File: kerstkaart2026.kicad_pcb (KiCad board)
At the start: 2 copper layers, 96 x 98.4 mm, 60 parts, among them SW1 TS-1187A-B-A-B, U1 ATtiny1616-MNR (VQFN-20)

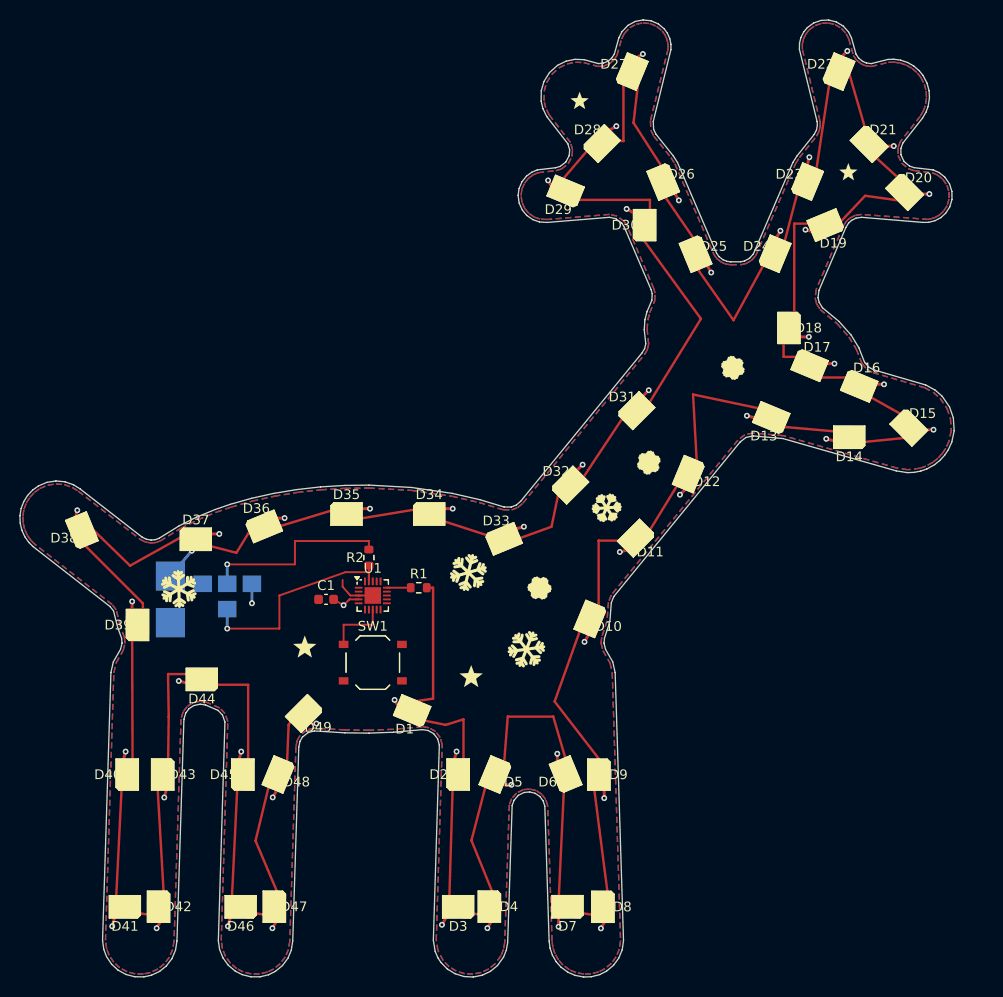
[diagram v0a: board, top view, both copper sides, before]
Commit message: Kerstkaart 2026 v3: SK6805-EC15 LED's, chip als oog, knop als neus, grote batterijpads + JST, rechte LED's, symmetrische geweien
Co-Authored-By: Claude Sonnet 5.5 <noreply@anthropic.com>
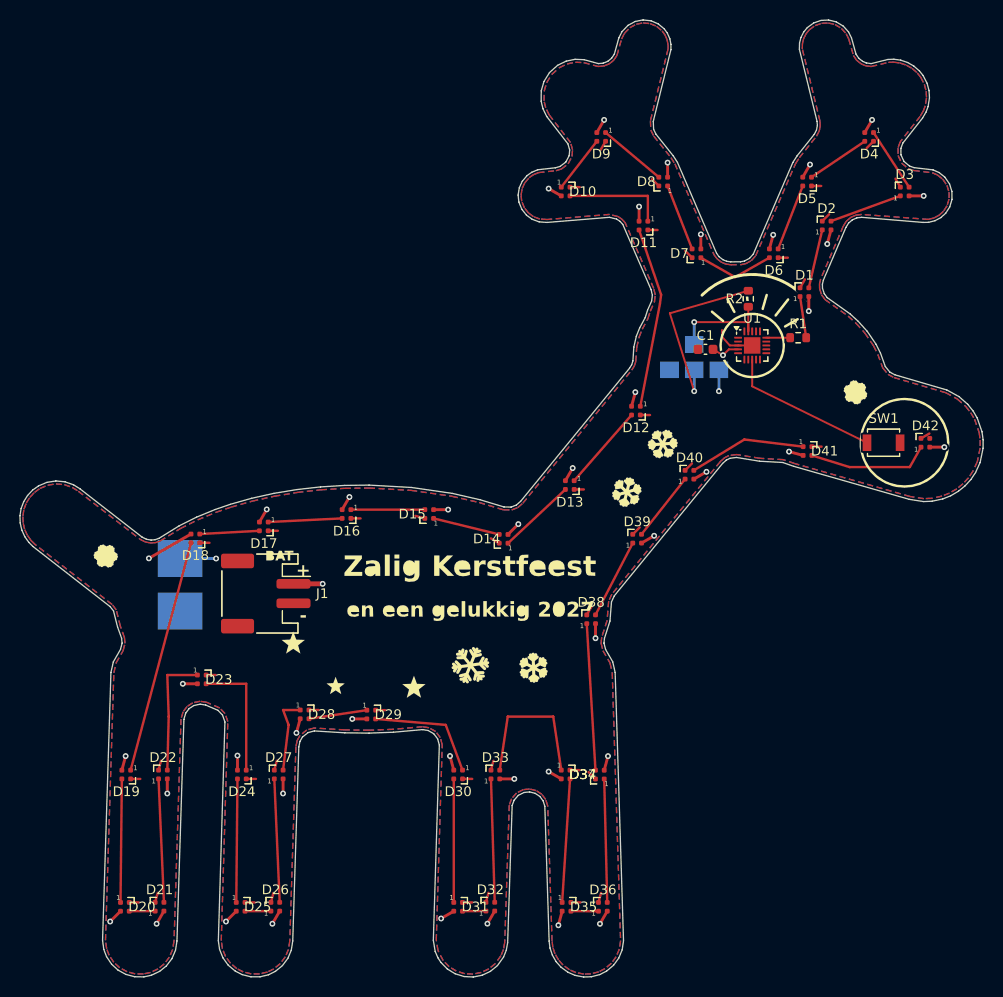
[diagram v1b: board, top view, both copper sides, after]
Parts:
- removed D43, D44, D45, D46, D47, D48, D49: WS2812B-2020, kerstkaart:LED_WS2812B-2020_PLCC4_2.0x2.0mm
- added J1: S2B-PH-SM4-TB(LF)(SN), kerstkaart:JST_PH_S2B-PH-SM4-TB_1x02-1MP_P2.00mm_Horizontal, F.Cu at (44.0, 101.0)
- D1, D10, D11, D12, D13, D14, D15, D16, D17, D18, D19, D2, D20, D21, D22, D23, D24, D25, D26, D27, D28, D29, D3, D30, D31, D32, D33, D34, D35, D36, D37, D38, D39, D4, D40, D41, D42, D5, D6, D7, D8, D9: value WS2812B-2020 -> SK6805-EC15; footprint kerstkaart:LED_WS2812B-2020_PLCC4_2.0x2.0mm -> kerstkaart:LED_SK6812_EC15_1.5x1.5mm
- SW1: value TS-1187A-B-A-B -> B3U-1000P; footprint kerstkaart:SW_Push_1P1T_XKB_TS-1187A -> kerstkaart:SW_SPST_B3U-1000P
- moved D20 108.8 mm to (29.5, 133.2), turned to 270 degrees
- moved D21 107.1 mm to (33.1, 133.2), turned to 0 degrees
- moved D22 100.2 mm to (33.4, 119.6), turned to 0 degrees
- moved D42 92.1 mm to (111.8, 85.5), turned to 0 degrees
- moved D19 91.4 mm to (29.7, 119.6), turned to 180 degrees
- moved D4 88.2 mm to (106.0, 54.1), turned to 180 degrees
- moved D3 86.7 mm to (109.7, 59.7), turned to 0 degrees
- moved D26 84.5 mm to (45.0, 133.2), turned to 0 degrees
- moved D41 84.4 mm to (99.7, 86.4), turned to 270 degrees
- moved D25 81.8 mm to (41.4, 133.2), turned to 270 degrees
- moved D27 80.9 mm to (45.3, 119.6), turned to 0 degrees
- moved D23 80.6 mm to (37.4, 109.8), turned to 270 degrees
- moved D24 76.6 mm to (41.5, 119.6), turned to 180 degrees
- moved D8 74.8 mm to (84.9, 58.7), turned to 90 degrees
- moved D5 68.9 mm to (99.6, 58.7), turned to 180 degrees
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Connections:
- D1 pad 1: D1 -> DATA1
- D1 pad 2: GND -> VCC
- D1 pad 3: DATA1 -> D1
- D1 pad 4: VCC -> GND
- D10 pad 1: D10 -> D9
- D10 pad 2: GND -> VCC
- D10 pad 3: D9 -> D10
- D10 pad 4: VCC -> GND
- D11 pad 1: D11 -> D10
- D11 pad 2: GND -> VCC
- D11 pad 3: D10 -> D11
- D11 pad 4: VCC -> GND
- D12 pad 1: D12 -> D11
- D12 pad 2: GND -> VCC
- D12 pad 3: D11 -> D12
- D12 pad 4: VCC -> GND
- D13 pad 1: D13 -> D12
- D13 pad 2: GND -> VCC
- D13 pad 3: D12 -> D13
- D13 pad 4: VCC -> GND
- D14 pad 1: D14 -> D13
- D14 pad 2: GND -> VCC
- D14 pad 3: D13 -> D14
- D14 pad 4: VCC -> GND
- D15 pad 1: D15 -> D14
- D15 pad 2: GND -> VCC
- D15 pad 3: D14 -> D15
- D15 pad 4: VCC -> GND
- D16 pad 1: D16 -> D15
- D16 pad 2: GND -> VCC
- D16 pad 3: D15 -> D16
- D16 pad 4: VCC -> GND
- D17 pad 1: D17 -> D16
- D17 pad 2: GND -> VCC
- D17 pad 3: D16 -> D17
- D17 pad 4: VCC -> GND
- D18 pad 1: D18 -> D17
- D18 pad 2: GND -> VCC
- D18 pad 3: D17 -> D18
- D18 pad 4: VCC -> GND
- D19 pad 1: D19 -> D18
- D19 pad 2: GND -> VCC
- D19 pad 3: D18 -> D19
- D19 pad 4: VCC -> GND
- D2 pad 1: D2 -> D1
- D2 pad 2: GND -> VCC
- D2 pad 3: D1 -> D2
- D2 pad 4: VCC -> GND
- D20 pad 1: D20 -> D19
- D20 pad 2: GND -> VCC
- D20 pad 3: D19 -> D20
- D20 pad 4: VCC -> GND
- D21 pad 1: D21 -> D20
- D21 pad 2: GND -> VCC
- D21 pad 3: D20 -> D21
- D21 pad 4: VCC -> GND
- D22 pad 1: D22 -> D21
- D22 pad 2: GND -> VCC
- D22 pad 3: D21 -> D22
- D22 pad 4: VCC -> GND
- D23 pad 1: D23 -> D22
- D23 pad 2: GND -> VCC
- D23 pad 3: D22 -> D23
- D23 pad 4: VCC -> GND
- D24 pad 1: D24 -> D23
- D24 pad 2: GND -> VCC
- D24 pad 3: D23 -> D24
- D24 pad 4: VCC -> GND
- D25 pad 1: D25 -> D24
- D25 pad 2: GND -> VCC
- D25 pad 3: D24 -> D25
- D25 pad 4: VCC -> GND
- D26 pad 1: D26 -> D25
- D26 pad 2: GND -> VCC
- D26 pad 3: D25 -> D26
- D26 pad 4: VCC -> GND
- D27 pad 1: D27 -> D26
- D27 pad 2: GND -> VCC
- D27 pad 3: D26 -> D27
- D27 pad 4: VCC -> GND
- D28 pad 1: D28 -> D27
- D28 pad 2: GND -> VCC
- D28 pad 3: D27 -> D28
- D28 pad 4: VCC -> GND
- D29 pad 1: D29 -> D28
- D29 pad 2: GND -> VCC
- D29 pad 3: D28 -> D29
- D29 pad 4: VCC -> GND
- D3 pad 1: D3 -> D2
- D3 pad 2: GND -> VCC
- D3 pad 3: D2 -> D3
- D3 pad 4: VCC -> GND
- D30 pad 1: D30 -> D29
- D30 pad 2: GND -> VCC
- D30 pad 3: D29 -> D30
- D30 pad 4: VCC -> GND
- D31 pad 1: D31 -> D30
- D31 pad 2: GND -> VCC
- D31 pad 3: D30 -> D31
- D31 pad 4: VCC -> GND
- D32 pad 1: D32 -> D31
- D32 pad 2: GND -> VCC
- D32 pad 3: D31 -> D32
- D32 pad 4: VCC -> GND
- D33 pad 1: D33 -> D32
- D33 pad 2: GND -> VCC
- D33 pad 3: D32 -> D33
- D33 pad 4: VCC -> GND
- D34 pad 1: D34 -> D33
- D34 pad 2: GND -> VCC
- D34 pad 3: D33 -> D34
- D34 pad 4: VCC -> GND
- D35 pad 1: D35 -> D34
- D35 pad 2: GND -> VCC
- D35 pad 3: D34 -> D35
- D35 pad 4: VCC -> GND
- D36 pad 1: D36 -> D35
- D36 pad 2: GND -> VCC
- D36 pad 3: D35 -> D36
- D36 pad 4: VCC -> GND
- D37 pad 1: D37 -> D36
- D37 pad 2: GND -> VCC
- D37 pad 3: D36 -> D37
- D37 pad 4: VCC -> GND
- D38 pad 1: D38 -> D37
- D38 pad 2: GND -> VCC
- D38 pad 3: D37 -> D38
- D38 pad 4: VCC -> GND
- D39 pad 1: D39 -> D38
- D39 pad 2: GND -> VCC
- D39 pad 3: D38 -> D39
- D39 pad 4: VCC -> GND
- D4 pad 1: D4 -> D3
- D4 pad 2: GND -> VCC
- D4 pad 3: D3 -> D4
- D4 pad 4: VCC -> GND
- D40 pad 1: D40 -> D39
- D40 pad 2: GND -> VCC
- D40 pad 3: D39 -> D40
- D40 pad 4: VCC -> GND
- D41 pad 1: D41 -> D40
- D41 pad 2: GND -> VCC
- D41 pad 3: D40 -> D41
- D41 pad 4: VCC -> GND
- D42 pad 1: D42 -> D41
- D42 pad 2: GND -> VCC
- D42 pad 3: D41 -> (no net)
- D42 pad 4: VCC -> GND
- D5 pad 1: D5 -> D4
- D5 pad 2: GND -> VCC
- D5 pad 3: D4 -> D5
- D5 pad 4: VCC -> GND
- D6 pad 1: D6 -> D5
- D6 pad 2: GND -> VCC
- D6 pad 3: D5 -> D6
- D6 pad 4: VCC -> GND
- D7 pad 1: D7 -> D6
- D7 pad 2: GND -> VCC
- D7 pad 3: D6 -> D7
- D7 pad 4: VCC -> GND
- D8 pad 1: D8 -> D7
- D8 pad 2: GND -> VCC
- D8 pad 3: D7 -> D8
- D8 pad 4: VCC -> GND
- D9 pad 1: D9 -> D8
- D9 pad 2: GND -> VCC
- D9 pad 3: D8 -> D9
- D9 pad 4: VCC -> GND
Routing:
- net GND: track 9.11 -> 51.6 mm
- net D47: track 12.7 -> 0.00 mm
- net D18: track 12.0 -> 24.2 mm
- net D44: track 12.2 -> 0.00 mm
- net D45: track 12.1 -> 0.00 mm
- net D11: track 6.66 -> 18.7 mm
- net D43: track 12.0 -> 0.00 mm
- net D42: track 11.8 -> 0.00 mm
- net UPDI0: track 22.9 -> 11.3 mm
- net D9: track 16.7 -> 5.96 mm
- net DATA1: track 14.9 -> 4.27 mm
- net D41: track 2.03 -> 12.6 mm
- net D33: track 5.97 -> 15.8 mm
- net BTN: track 6.57 -> 15.9 mm
- net D30: track 21.6 -> 12.7 mm
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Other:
- board size 96 x 98.4 mm -> 99 x 98.4 mm

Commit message: v4: JST weg, LED-padafstanden gerepareerd, koper tot aan de rand
Co-Authored-By: Claude Sonnet 5.5 <noreply@anthropic.com>
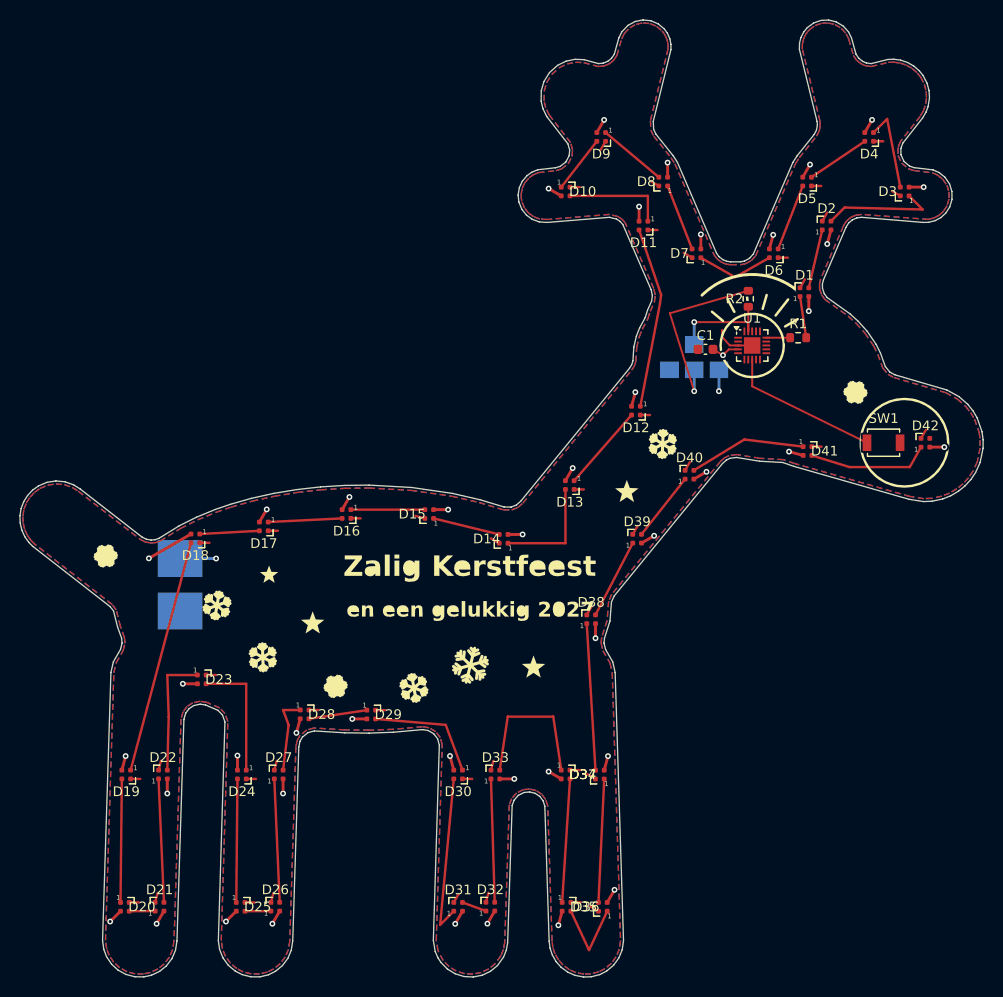
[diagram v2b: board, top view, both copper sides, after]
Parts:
- removed J1: S2B-PH-SM4-TB(LF)(SN), kerstkaart:JST_PH_S2B-PH-SM4-TB_1x02-1MP_P2.00mm_Horizontal
- turned D3 to 90 degrees
- turned D31 to 0 degrees
- turned D36 to 90 degrees
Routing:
- net D35: track 2.83 -> 8.83 mm
- net D2: track 7.58 -> 12.0 mm
- net D30: track 12.7 -> 17.0 mm
- net D13: track 8.08 -> 11.4 mm
- net VCC: track 72.5 -> 69.5 mm, vias 44 -> 43
- net D3: track 6.70 -> 9.12 mm

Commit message: v5: GND-via's, tekst vrij van LED's, randkoper, geen ref-teksten in KiCad
Co-Authored-By: Claude Sonnet 5.5 <noreply@anthropic.com>
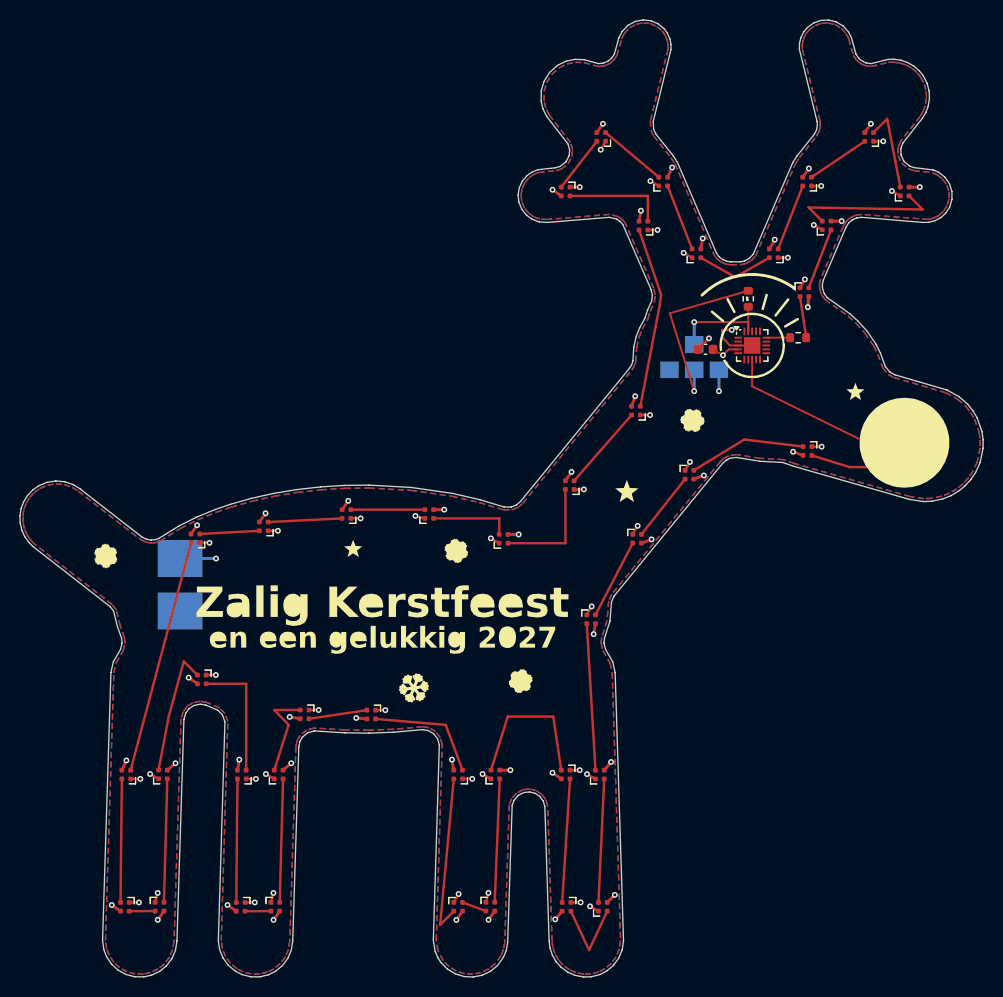
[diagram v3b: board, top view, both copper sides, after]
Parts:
- turned D2 to 90 degrees
- turned D22 to 90 degrees
- turned D27 to 90 degrees
- turned D33 to 90 degrees
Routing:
- net VCC: track 69.5 -> 49.2 mm
- net D2: track 12.0 -> 15.7 mm
- net GND: track 51.6 -> 55.2 mm, vias 2 -> 47
- net D27: track 8.08 -> 9.66 mm
- net D14: track 6.95 -> 8.40 mm
- net D22: track 12.9 -> 13.5 mm
